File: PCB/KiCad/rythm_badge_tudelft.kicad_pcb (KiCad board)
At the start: 2 copper layers, 35 x 47 mm, 42 parts, among them J1 10118194-0001LF, J2 SWD, J3 503182-1852, J4 BAT+, J5 BAT-, SW1 OFF-ON, SW2 OFF-LOW-HI, U1 TP4057, U2 MP34DT05-A, U3 MP34DT05-A, U4 AP7345D, U5 ICM-20948, U6 NTS0104, U7 MP34DT05-A

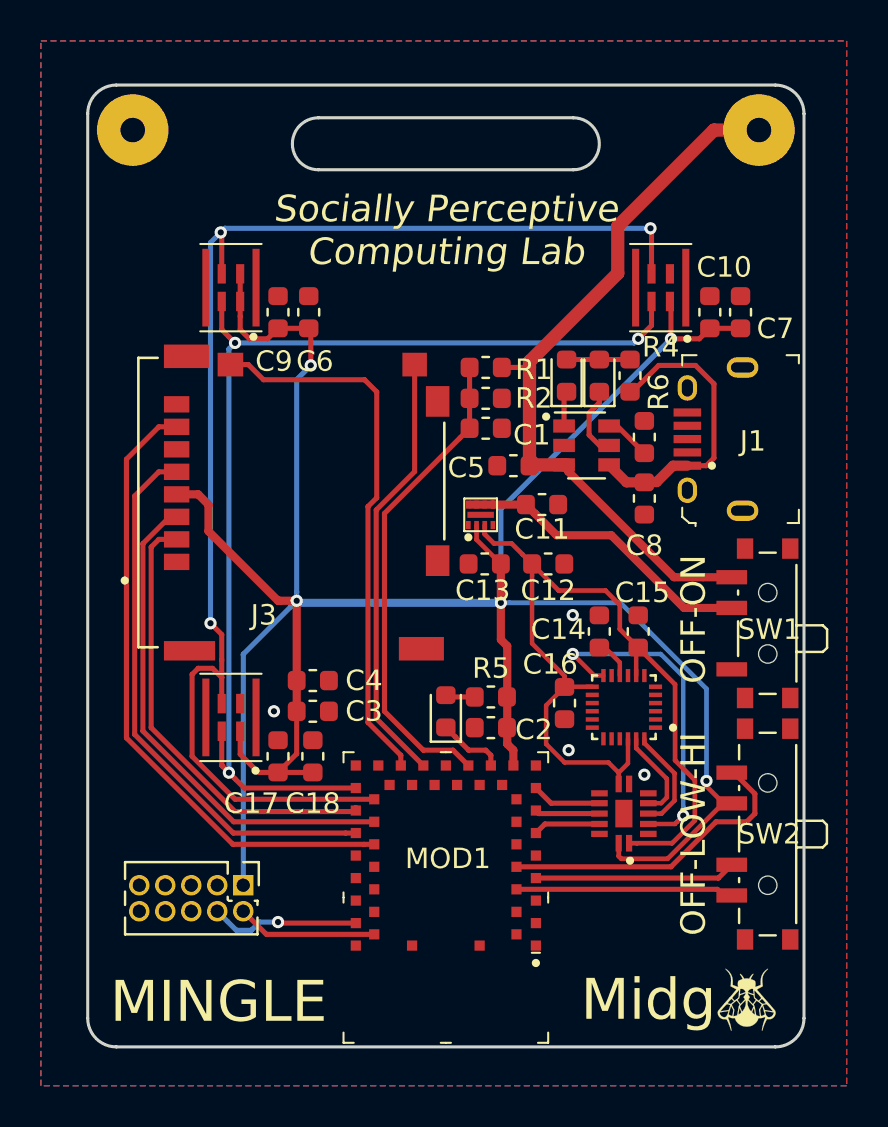
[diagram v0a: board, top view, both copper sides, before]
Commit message: Replace most of placeholders, add links to readme
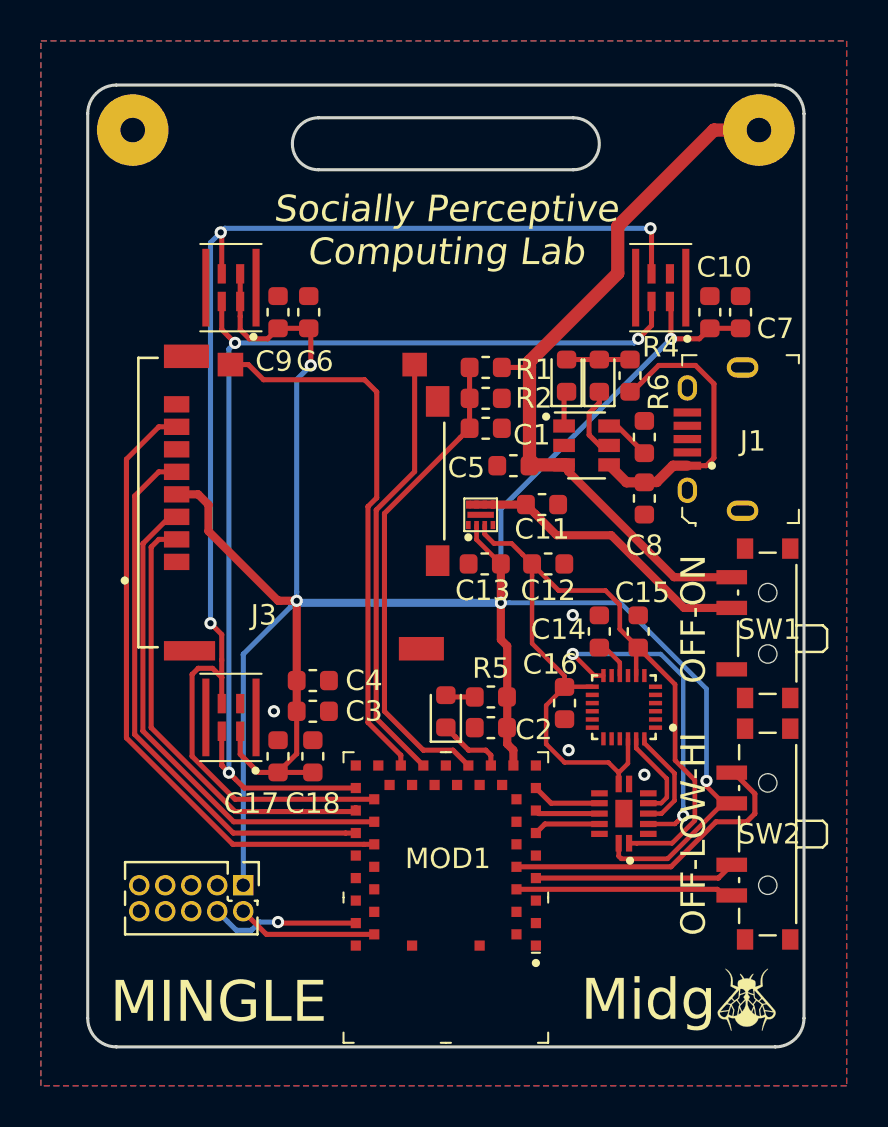
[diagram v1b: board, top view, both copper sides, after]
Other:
- net class 3V3 removed
- net class BAT removed
- net class Default removed
- net class Power removed
